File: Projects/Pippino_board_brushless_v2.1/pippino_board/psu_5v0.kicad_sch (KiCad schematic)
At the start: 4 parts, among them U7 CK1408

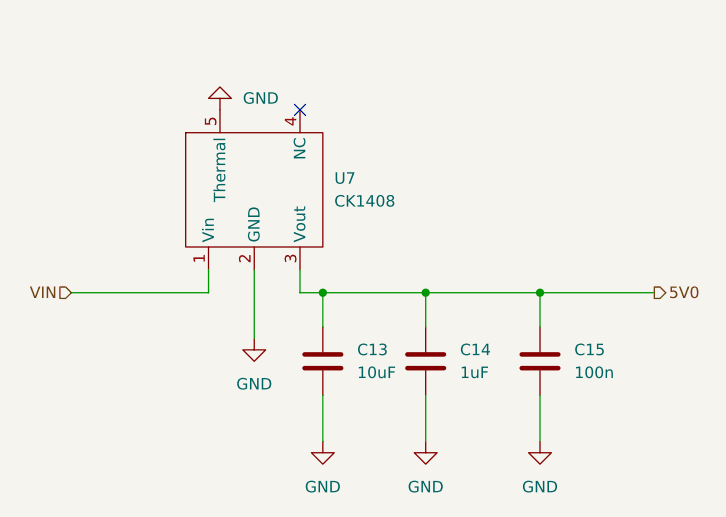
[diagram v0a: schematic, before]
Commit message: changed 5v buck to smaller one
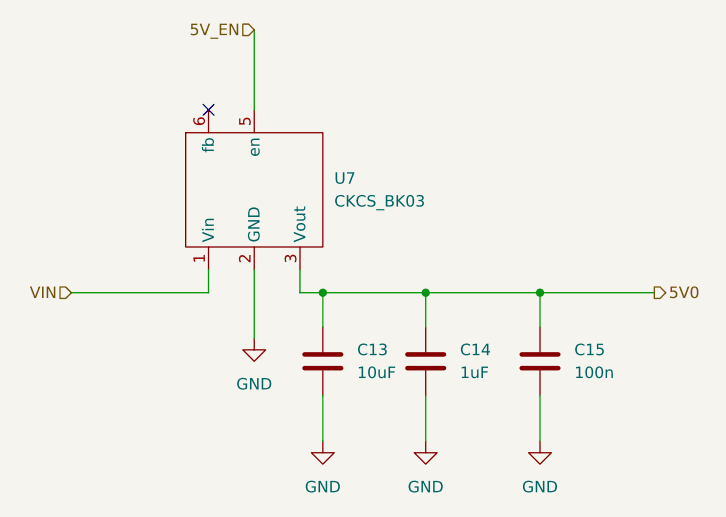
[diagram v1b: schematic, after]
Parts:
- U7: value CK1408 -> CKCS_BK03; footprint Pcb_Modules:CK1408 -> pcb_modules:CKCS_BK03; symbol pcb_modules:CK1408 -> pcb_modules:CKCS_BK03
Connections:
- net GND: no longer U7.5 (Thermal)
- new net 5V_EN: U7.5 (en)
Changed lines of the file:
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@@
   (junction (at 151.13 87.63) (diameter 0) (color 0 0 0 0)
   )
-  (no_connect (at 137.16 67.31))
+  (no_connect (at 127 67.31))
   (wire (pts (xy 163.83 87.63) (xy 176.53 87.63))
     (stroke (width 0) (type default))
@@
   )
   (wire (pts (xy 151.13 87.63) (xy 151.13 91.44))
+    (stroke (width 0) (type default))
+  )
+  (wire (pts (xy 132.08 58.42) (xy 132.08 67.31))
     (stroke (width 0) (type default))
   )
@@
     (effects (font (size 1.27 1.27)) (justify right))
   )
+  (hierarchical_label "5V_EN" (shape input) (at 132.08 58.42 180) (fields_autoplaced)
+    (effects (font (size 1.27 1.27)) (justify right))
+  )
   (hierarchical_label "5V0" (shape output) (at 176.53 87.63 0) (fields_autoplaced)
     (effects (font (size 1.27 1.27)) (justify left))
@@
     )
   )
-  (symbol (lib_id "power:GND") (at 128.27 67.31 180) (unit 1)
-    (in_bom yes) (on_board yes) (dnp no) (fields_autoplaced)
-    (property "Reference" "#PWR0102" (at 128.27 60.96 0)
-      (effects (font (size 1.27 1.27)) hide)
-    )
-    (property "Value" "GND" (at 130.81 66.0399 0)
-      (effects (font (size 1.27 1.27)) (justify right))
-    )
-    (property "Footprint" "" (at 128.27 67.31 0)
-      (effects (font (size 1.27 1.27)) hide)
-    )
-    (property "Datasheet" "" (at 128.27 67.31 0)
-      (effects (font (size 1.27 1.27)) hide)
-    )
-    (pin "1")
-    (instances
-      (project "pippino_board"
-        (path "/dedb2da3-2254-430c-8837-0c4d082ac264/4b10fb5e-e57c-48de-8995-e07357b61829/bd5f091a-3a64-41f8-8f2e-75fdc82bab1f"
-          (reference "#PWR0102") (unit 1)
-        )
-      )
-    )
-  )
   (symbol (lib_id "Device:C") (at 151.13 95.25 0) (unit 1)
     (in_bom yes) (on_board yes) (dnp no) (fields_autoplaced)
@@
     )
   )
-  (symbol (lib_id "pcb_modules:CK1408") (at 132.08 76.2 0) (unit 1)
+  (symbol (lib_id "pcb_modules:CKCS_BK03") (at 132.08 76.2 0) (unit 1)
     (in_bom yes) (on_board yes) (dnp no) (fields_autoplaced)
     (property "Reference" "U7" (at 140.97 74.9299 0)
       (effects (font (size 1.27 1.27)) (justify left))
     )
-    (property "Value" "CK1408" (at 140.97 77.4699 0)
-      (effects (font (size 1.27 1.27)) (justify left))
-    )
-    (property "Footprint" "Pcb_Modules:CK1408" (at 132.08 76.2 0)
+    (property "Value" "CKCS_BK03" (at 140.97 77.4699 0)
+      (effects (font (size 1.27 1.27)) (justify left))
+    )
+    (property "Footprint" "pcb_modules:CKCS_BK03" (at 132.08 76.2 0)
       (effects (font (size 1.27 1.27)) hide)
     )
     (property "Datasheet" "" (at 132.08 76.2 0)
+      (effects (font (size 1.27 1.27)) hide)
+    )
+    (property "Field4" "" (at 132.08 76.2 0)
+      (effects (font (size 1.27 1.27)) hide)
+    )
+    (property "Field5" "" (at 132.08 76.2 0)
       (effects (font (size 1.27 1.27)) hide)
     )
@@
     (pin "4")
     (pin "5")
-    (pin "1")
-    (instances
+    (pin "6")
+    (pin "1")
+    (instances

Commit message: moved to ubu 22, updated pippino v2.1
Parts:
- U7: footprint pcb_modules:CKCS_BK03 -> Pcb_Modules:CKCS-BK03
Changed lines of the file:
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@@
       (effects (font (size 1.27 1.27)) (justify left))
     )
-    (property "Footprint" "pcb_modules:CKCS_BK03" (at 132.08 76.2 0)
+    (property "Footprint" "Pcb_Modules:CKCS-BK03" (at 132.08 76.2 0)
       (effects (font (size 1.27 1.27)) hide)
     )
